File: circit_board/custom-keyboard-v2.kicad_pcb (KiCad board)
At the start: 2 copper layers, 4 parts, among them SW1 SW_Push

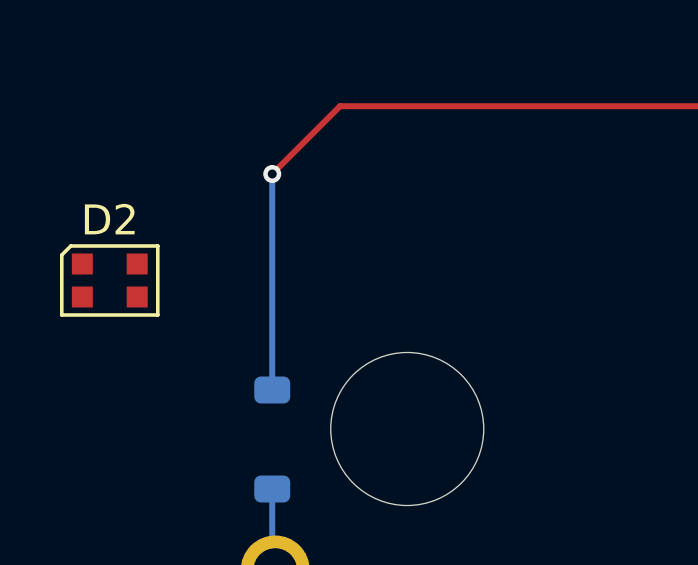
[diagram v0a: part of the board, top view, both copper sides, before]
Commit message: Added instructions for centering an LED + gitignore
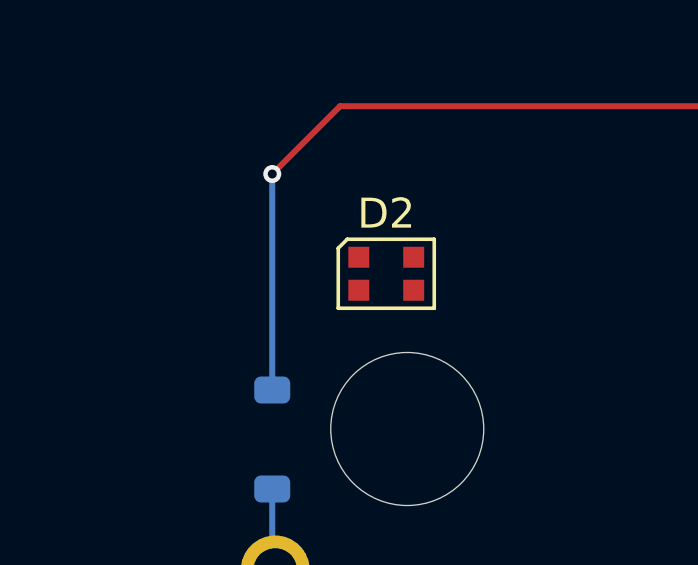
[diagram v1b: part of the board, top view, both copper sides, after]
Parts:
- moved D2 9.22 mm to (122.3, 78.3)
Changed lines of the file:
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@@
 	(footprint "LED_SMD:LED_WS2812B-2020_PLCC4_2.0x2.0mm"
 		(layer "F.Cu")
-		(at 113.085 78.55)
+		(at 122.3 78.325)
 		(descr "2.0mm x 2.0mm Addressable RGB LED NeoPixel Nano, 12 mA, https://cdn-shop.adafruit.com/product-files/4684/4684_WS2812B-2020_V1.3_EN.pdf")
 		(tags "LED RGB NeoPixel Nano PLCC-4 2020")

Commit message: Possitioned keys on circitboard with spacing of 19mm (may change later)
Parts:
- added D10: 1N4148W, Diode_SMD:D_SOD-123, F.Cu at (58.6, 191.1)
- added D11: 1N4148W, Diode_SMD:D_SOD-123, F.Cu at (64.4, 160.9)
- added D12: 1N4148W, Diode_SMD:D_SOD-123, F.Cu at (64.4, 164.3)
- added D13: 1N4148W, Diode_SMD:D_SOD-123, F.Cu at (64.4, 167.7)
- added D14: 1N4148W, Diode_SMD:D_SOD-123, F.Cu at (64.4, 171.0)
- added D15: 1N4148W, Diode_SMD:D_SOD-123, F.Cu at (64.4, 174.3)
- added D16: 1N4148W, Diode_SMD:D_SOD-123, F.Cu at (64.4, 177.7)
- added D17: 1N4148W, Diode_SMD:D_SOD-123, F.Cu at (64.4, 181.1)
- added D18: 1N4148W, Diode_SMD:D_SOD-123, F.Cu at (64.4, 184.4)
- added D19: 1N4148W, Diode_SMD:D_SOD-123, F.Cu at (64.4, 187.8)
- added D20: 1N4148W, Diode_SMD:D_SOD-123, F.Cu at (64.4, 191.1)
- added D21: 1N4148W, Diode_SMD:D_SOD-123, F.Cu at (70.2, 160.9)
- added D22: 1N4148W, Diode_SMD:D_SOD-123, F.Cu at (70.2, 164.3)
- added D23: 1N4148W, Diode_SMD:D_SOD-123, F.Cu at (70.2, 167.7)
- added D24: 1N4148W, Diode_SMD:D_SOD-123, F.Cu at (70.2, 171.0)
- added D25: 1N4148W, Diode_SMD:D_SOD-123, F.Cu at (70.2, 174.3)
- added D26: 1N4148W, Diode_SMD:D_SOD-123, F.Cu at (70.2, 177.7)
- added D27: 1N4148W, Diode_SMD:D_SOD-123, F.Cu at (70.2, 181.1)
- added D28: 1N4148W, Diode_SMD:D_SOD-123, F.Cu at (70.2, 184.4)
- added D29: 1N4148W, Diode_SMD:D_SOD-123, F.Cu at (70.2, 187.8)
- added D3: 1N4148W, Diode_SMD:D_SOD-123, F.Cu at (58.6, 167.7)
- added D30: 1N4148W, Diode_SMD:D_SOD-123, F.Cu at (70.2, 191.1)
- added D31: 1N4148W, Diode_SMD:D_SOD-123, F.Cu at (76.0, 160.9)
- added D32: 1N4148W, Diode_SMD:D_SOD-123, F.Cu at (76.0, 164.3)
- added D33: 1N4148W, Diode_SMD:D_SOD-123, F.Cu at (76.0, 167.7)
- added D34: 1N4148W, Diode_SMD:D_SOD-123, F.Cu at (76.0, 171.0)
- added D35: 1N4148W, Diode_SMD:D_SOD-123, F.Cu at (76.0, 174.3)
- added D36: 1N4148W, Diode_SMD:D_SOD-123, F.Cu at (76.0, 177.7)
- added D37: 1N4148W, Diode_SMD:D_SOD-123, F.Cu at (76.0, 181.1)
- added D38: 1N4148W, Diode_SMD:D_SOD-123, F.Cu at (76.0, 184.4)
- added D39: 1N4148W, Diode_SMD:D_SOD-123, F.Cu at (76.0, 187.8)
- added D4: 1N4148W, Diode_SMD:D_SOD-123, F.Cu at (58.6, 171.0)
- added D40: 1N4148W, Diode_SMD:D_SOD-123, F.Cu at (76.0, 191.1)
- added D41: 1N4148W, Diode_SMD:D_SOD-123, F.Cu at (81.8, 160.9)
- added D42: 1N4148W, Diode_SMD:D_SOD-123, F.Cu at (81.8, 164.3)
- added D43: 1N4148W, Diode_SMD:D_SOD-123, F.Cu at (81.8, 167.7)
- added D44: 1N4148W, Diode_SMD:D_SOD-123, F.Cu at (81.8, 171.0)
- added D45: 1N4148W, Diode_SMD:D_SOD-123, F.Cu at (81.8, 174.3)
- added D46: 1N4148W, Diode_SMD:D_SOD-123, F.Cu at (81.8, 177.7)
- added D5: 1N4148W, Diode_SMD:D_SOD-123, F.Cu at (58.6, 174.3)
- added D6: 1N4148W, Diode_SMD:D_SOD-123, F.Cu at (58.6, 177.7)
- added D7: 1N4148W, Diode_SMD:D_SOD-123, F.Cu at (58.6, 181.1)
- added D8: 1N4148W, Diode_SMD:D_SOD-123, F.Cu at (58.6, 184.4)
- added D9: 1N4148W, Diode_SMD:D_SOD-123, F.Cu at (58.6, 187.8)
- added LED1: WS2812B-2020, LED_SMD:LED_WS2812B-2020_PLCC4_2.0x2.0mm, F.Cu at (86.9, 161.1)
- added LED10: WS2812B-2020, LED_SMD:LED_WS2812B-2020_PLCC4_2.0x2.0mm, F.Cu at (91.2, 164.6)
- added LED11: WS2812B-2020, LED_SMD:LED_WS2812B-2020_PLCC4_2.0x2.0mm, F.Cu at (91.2, 168.2)
- added LED12: WS2812B-2020, LED_SMD:LED_WS2812B-2020_PLCC4_2.0x2.0mm, F.Cu at (91.2, 171.7)
- added LED13: WS2812B-2020, LED_SMD:LED_WS2812B-2020_PLCC4_2.0x2.0mm, F.Cu at (91.2, 175.2)
- added LED14: WS2812B-2020, LED_SMD:LED_WS2812B-2020_PLCC4_2.0x2.0mm, F.Cu at (91.2, 178.8)
- added LED15: WS2812B-2020, LED_SMD:LED_WS2812B-2020_PLCC4_2.0x2.0mm, F.Cu at (91.2, 182.3)
- added LED16: WS2812B-2020, LED_SMD:LED_WS2812B-2020_PLCC4_2.0x2.0mm, F.Cu at (91.2, 185.9)
- added LED17: WS2812B-2020, LED_SMD:LED_WS2812B-2020_PLCC4_2.0x2.0mm, F.Cu at (95.5, 161.1)
- added LED18: WS2812B-2020, LED_SMD:LED_WS2812B-2020_PLCC4_2.0x2.0mm, F.Cu at (95.5, 164.6)
- added LED19: WS2812B-2020, LED_SMD:LED_WS2812B-2020_PLCC4_2.0x2.0mm, F.Cu at (95.5, 168.2)
- added LED2: WS2812B-2020, LED_SMD:LED_WS2812B-2020_PLCC4_2.0x2.0mm, F.Cu at (86.9, 164.6)
- added LED20: WS2812B-2020, LED_SMD:LED_WS2812B-2020_PLCC4_2.0x2.0mm, F.Cu at (95.5, 171.7)
- added LED21: WS2812B-2020, LED_SMD:LED_WS2812B-2020_PLCC4_2.0x2.0mm, F.Cu at (95.5, 175.2)
- added LED22: WS2812B-2020, LED_SMD:LED_WS2812B-2020_PLCC4_2.0x2.0mm, F.Cu at (95.5, 178.8)
- added LED23: WS2812B-2020, LED_SMD:LED_WS2812B-2020_PLCC4_2.0x2.0mm, F.Cu at (95.5, 182.3)
- added LED24: WS2812B-2020, LED_SMD:LED_WS2812B-2020_PLCC4_2.0x2.0mm, F.Cu at (95.5, 185.9)
- added LED25: WS2812B-2020, LED_SMD:LED_WS2812B-2020_PLCC4_2.0x2.0mm, F.Cu at (99.8, 161.1)
- added LED26: WS2812B-2020, LED_SMD:LED_WS2812B-2020_PLCC4_2.0x2.0mm, F.Cu at (99.8, 164.6)
- added LED27: WS2812B-2020, LED_SMD:LED_WS2812B-2020_PLCC4_2.0x2.0mm, F.Cu at (99.8, 168.2)
- added LED28: WS2812B-2020, LED_SMD:LED_WS2812B-2020_PLCC4_2.0x2.0mm, F.Cu at (99.8, 171.7)
- added LED29: WS2812B-2020, LED_SMD:LED_WS2812B-2020_PLCC4_2.0x2.0mm, F.Cu at (99.8, 175.2)
- added LED3: WS2812B-2020, LED_SMD:LED_WS2812B-2020_PLCC4_2.0x2.0mm, F.Cu at (86.9, 168.2)
- added LED30: WS2812B-2020, LED_SMD:LED_WS2812B-2020_PLCC4_2.0x2.0mm, F.Cu at (99.8, 178.8)
- added LED31: WS2812B-2020, LED_SMD:LED_WS2812B-2020_PLCC4_2.0x2.0mm, F.Cu at (99.8, 182.3)
- added LED32: WS2812B-2020, LED_SMD:LED_WS2812B-2020_PLCC4_2.0x2.0mm, F.Cu at (99.8, 185.9)
- added LED33: WS2812B-2020, LED_SMD:LED_WS2812B-2020_PLCC4_2.0x2.0mm, F.Cu at (104.1, 161.1)
- added LED34: WS2812B-2020, LED_SMD:LED_WS2812B-2020_PLCC4_2.0x2.0mm, F.Cu at (104.1, 164.6)
- added LED35: WS2812B-2020, LED_SMD:LED_WS2812B-2020_PLCC4_2.0x2.0mm, F.Cu at (104.1, 168.2)
- added LED36: WS2812B-2020, LED_SMD:LED_WS2812B-2020_PLCC4_2.0x2.0mm, F.Cu at (104.1, 171.7)
- added LED37: WS2812B-2020, LED_SMD:LED_WS2812B-2020_PLCC4_2.0x2.0mm, F.Cu at (104.1, 175.2)
- added LED38: WS2812B-2020, LED_SMD:LED_WS2812B-2020_PLCC4_2.0x2.0mm, F.Cu at (104.1, 178.8)
- added LED39: WS2812B-2020, LED_SMD:LED_WS2812B-2020_PLCC4_2.0x2.0mm, F.Cu at (104.1, 182.3)
- added LED4: WS2812B-2020, LED_SMD:LED_WS2812B-2020_PLCC4_2.0x2.0mm, F.Cu at (86.9, 171.7)
- added LED40: WS2812B-2020, LED_SMD:LED_WS2812B-2020_PLCC4_2.0x2.0mm, F.Cu at (104.1, 185.9)
- added LED41: WS2812B-2020, LED_SMD:LED_WS2812B-2020_PLCC4_2.0x2.0mm, F.Cu at (108.5, 161.1)
- added LED42: WS2812B-2020, LED_SMD:LED_WS2812B-2020_PLCC4_2.0x2.0mm, F.Cu at (108.5, 164.6)
- added LED43: WS2812B-2020, LED_SMD:LED_WS2812B-2020_PLCC4_2.0x2.0mm, F.Cu at (108.5, 168.2)
- added LED44: WS2812B-2020, LED_SMD:LED_WS2812B-2020_PLCC4_2.0x2.0mm, F.Cu at (108.5, 171.7)
- added LED45: WS2812B-2020, LED_SMD:LED_WS2812B-2020_PLCC4_2.0x2.0mm, F.Cu at (108.5, 175.2)
- added LED46: WS2812B-2020, LED_SMD:LED_WS2812B-2020_PLCC4_2.0x2.0mm, F.Cu at (108.5, 178.8)
- added LED5: WS2812B-2020, LED_SMD:LED_WS2812B-2020_PLCC4_2.0x2.0mm, F.Cu at (86.9, 175.2)
- added LED6: WS2812B-2020, LED_SMD:LED_WS2812B-2020_PLCC4_2.0x2.0mm, F.Cu at (86.9, 178.8)
- added LED7: WS2812B-2020, LED_SMD:LED_WS2812B-2020_PLCC4_2.0x2.0mm, F.Cu at (86.9, 182.3)
- added LED8: WS2812B-2020, LED_SMD:LED_WS2812B-2020_PLCC4_2.0x2.0mm, F.Cu at (86.9, 185.9)
- added LED9: WS2812B-2020, LED_SMD:LED_WS2812B-2020_PLCC4_2.0x2.0mm, F.Cu at (91.2, 161.1)
- added SW10: SW_Push, MX_V2:Gateron-KS33-Solderable-Template, F.Cu at (266.0, 57.0)
- added SW11: SW_Push, MX_V2:Gateron-KS33-Solderable-Template, F.Cu at (38.0, 76.0)
- added SW12: SW_Push, MX_V2:Gateron-KS33-Solderable-Template, F.Cu at (57.0, 76.0)
- added SW13: SW_Push, MX_V2:Gateron-KS33-Solderable-Template, F.Cu at (76.0, 76.0)
- added SW14: SW_Push, MX_V2:Gateron-KS33-Solderable-Template, F.Cu at (95.0, 76.0)
- added SW15: SW_Push, MX_V2:Gateron-KS33-Solderable-Template, F.Cu at (114.0, 76.0)
- added SW16: SW_Push, MX_V2:Gateron-KS33-Solderable-Template, F.Cu at (190.0, 76.0)
- added SW17: SW_Push, MX_V2:Gateron-KS33-Solderable-Template, F.Cu at (209.0, 76.0)
- added SW18: SW_Push, MX_V2:Gateron-KS33-Solderable-Template, F.Cu at (228.0, 76.0)
- added SW19: SW_Push, MX_V2:Gateron-KS33-Solderable-Template, F.Cu at (247.0, 76.0)
- added SW2: SW_Push, MX_V2:Gateron-KS33-Solderable-Template, F.Cu at (57.0, 57.0)
- added SW20: SW_Push, MX_V2:Gateron-KS33-Solderable-Template, F.Cu at (266.0, 76.0)
- added SW21: SW_Push, MX_V2:Gateron-KS33-Solderable-Template, F.Cu at (38.0, 95.0)
- added SW22: SW_Push, MX_V2:Gateron-KS33-Solderable-Template, F.Cu at (57.0, 95.0)
- added SW23: SW_Push, MX_V2:Gateron-KS33-Solderable-Template, F.Cu at (76.0, 95.0)
- added SW24: SW_Push, MX_V2:Gateron-KS33-Solderable-Template, F.Cu at (95.0, 95.0)
- added SW25: SW_Push, MX_V2:Gateron-KS33-Solderable-Template, F.Cu at (114.0, 95.0)
- added SW26: SW_Push, MX_V2:Gateron-KS33-Solderable-Template, F.Cu at (190.0, 95.0)
- added SW27: SW_Push, MX_V2:Gateron-KS33-Solderable-Template, F.Cu at (209.0, 95.0)
- added SW28: SW_Push, MX_V2:Gateron-KS33-Solderable-Template, F.Cu at (228.0, 95.0)
- added SW29: SW_Push, MX_V2:Gateron-KS33-Solderable-Template, F.Cu at (247.0, 95.0)
- added SW3: SW_Push, MX_V2:Gateron-KS33-Solderable-Template, F.Cu at (76.0, 57.0)
- added SW30: SW_Push, MX_V2:Gateron-KS33-Solderable-Template, F.Cu at (266.0, 95.0)
- added SW31: SW_Push, MX_V2:Gateron-KS33-Solderable-Template, F.Cu at (38.0, 114.0)
- added SW32: SW_Push, MX_V2:Gateron-KS33-Solderable-Template, F.Cu at (57.0, 114.0)
- added SW33: SW_Push, MX_V2:Gateron-KS33-Solderable-Template, F.Cu at (76.0, 114.0)
- added SW34: SW_Push, MX_V2:Gateron-KS33-Solderable-Template, F.Cu at (95.0, 114.0)
- added SW35: SW_Push, MX_V2:Gateron-KS33-Solderable-Template, F.Cu at (114.0, 114.0)
- added SW36: SW_Push, MX_V2:Gateron-KS33-Solderable-Template, F.Cu at (190.0, 114.0)
- added SW37: SW_Push, MX_V2:Gateron-KS33-Solderable-Template, F.Cu at (209.0, 114.0)
- added SW38: SW_Push, MX_V2:Gateron-KS33-Solderable-Template, F.Cu at (228.0, 114.0)
- added SW39: SW_Push, MX_V2:Gateron-KS33-Solderable-Template, F.Cu at (247.0, 114.0)
- added SW4: SW_Push, MX_V2:Gateron-KS33-Solderable-Template, F.Cu at (95.0, 57.0)
- added SW40: SW_Push, MX_V2:Gateron-KS33-Solderable-Template, F.Cu at (266.0, 114.0)
- added SW41: SW_Push, MX_V2:Gateron-KS33-Solderable-Template, F.Cu at (76.0, 133.0)
- added SW42: SW_Push, MX_V2:Gateron-KS33-Solderable-Template, F.Cu at (95.0, 133.0)
- added SW43: SW_Push, MX_V2:Gateron-KS33-Solderable-Template, F.Cu at (114.0, 133.0)
- added SW44: SW_Push, MX_V2:Gateron-KS33-Solderable-Template, F.Cu at (190.0, 133.0)
- added SW45: SW_Push, MX_V2:Gateron-KS33-Solderable-Template, F.Cu at (209.0, 133.0)
- added SW46: SW_Push, MX_V2:Gateron-KS33-Solderable-Template, F.Cu at (228.0, 133.0)
- added SW5: SW_Push, MX_V2:Gateron-KS33-Solderable-Template, F.Cu at (114.0, 57.0)
- added SW6: SW_Push, MX_V2:Gateron-KS33-Solderable-Template, F.Cu at (190.0, 57.0)
- added SW7: SW_Push, MX_V2:Gateron-KS33-Solderable-Template, F.Cu at (209.0, 57.0)
- added SW8: SW_Push, MX_V2:Gateron-KS33-Solderable-Template, F.Cu at (228.0, 57.0)
- added SW9: SW_Push, MX_V2:Gateron-KS33-Solderable-Template, F.Cu at (247.0, 57.0)
- D1: moved to F.Cu
- D2: value WS2812B-2020 -> 1N4148W; footprint LED_SMD:LED_WS2812B-2020_PLCC4_2.0x2.0mm -> Diode_SMD:D_SOD-123
- moved D2 107.0 mm to (58.6, 164.3)
- moved D1 97.6 mm to (58.6, 160.9), turned to 0 degrees
- moved SW1 89.0 mm to (38.0, 57.0)
- moved A1 21.6 mm to (152.0, 76.0)
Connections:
- A1 pad 1: Net-(A1-GPIO0) -> col1
- A1 pad 10: unconnected-(A1-GPIO7-Pad10) -> col8
- A1 pad 11: unconnected-(A1-GPIO8-Pad11) -> col9
- A1 pad 12: unconnected-(A1-GPIO9-Pad12) -> col10
- A1 pad 13: Net-(A1-GND-Pad13) -> gnd
- A1 pad 14: unconnected-(A1-GPIO10-Pad14) -> row1
- A1 pad 15: unconnected-(A1-GPIO11-Pad15) -> row2
- A1 pad 16: unconnected-(A1-GPIO12-Pad16) -> row3
- A1 pad 17: unconnected-(A1-GPIO13-Pad17) -> row4
- A1 pad 18: Net-(A1-GND-Pad13) -> gnd
- A1 pad 19: unconnected-(A1-GPIO14-Pad19) -> row5
- A1 pad 2: unconnected-(A1-GPIO1-Pad2) -> col2
- A1 pad 20: unconnected-(A1-GPIO15-Pad20) -> led-data
- A1 pad 23: Net-(A1-GND-Pad13) -> gnd
- A1 pad 28: Net-(A1-GND-Pad13) -> gnd
- A1 pad 3: Net-(A1-GND-Pad13) -> gnd
- A1 pad 38: Net-(A1-GND-Pad13) -> gnd
- A1 pad 4: unconnected-(A1-GPIO2-Pad4) -> col3
- A1 pad 40: unconnected-(A1-VBUS-Pad40) -> led-power
- A1 pad 5: unconnected-(A1-GPIO3-Pad5) -> col4
- A1 pad 6: unconnected-(A1-GPIO4-Pad6) -> col5
- A1 pad 7: unconnected-(A1-GPIO5-Pad7) -> col6
- A1 pad 8: Net-(A1-GND-Pad13) -> gnd
- A1 pad 9: unconnected-(A1-GPIO6-Pad9) -> col7
- D1 pad 1: Net-(D1-K) -> row1
- D1 pad 2: Net-(A1-GPIO0) -> Net-(D1-A)
- D2 pad 1: unconnected-(D2-DOUT-Pad1) -> row1
- D2 pad 2: unconnected-(D2-VSS-Pad2) -> Net-(D2-A)
- SW1 pad 1: Net-(D1-K) -> col1
- SW1 pad 2: Net-(A1-GND-Pad13) -> Net-(D1-A)
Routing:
- net Net-(A1-GPIO0): track 26.6 -> 0.00 mm, vias 1 -> 0
- net Net-(A1-GND-Pad13): track 11.8 -> 0.00 mm
- net Net-(D1-K): track 2.74 -> 0.00 mm

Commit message: Positioned dioes on circit board
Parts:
- D1, D10, D11, D12, D13, D14, D15, D16, D17, D18, D19, D2, D20, D21, D22, D23, D24, D25, D26, D27, D28, D29, D3, D30, D31, D32, D33, D34, D35, D36, D37, D38, D39, D4, D40, D41, D42, D43, D44, D45, D46, D5, D6, D7, D8, D9: moved to B.Cu
- moved D10 304.7 mm to (346.8, 91.9), turned to -90 degrees
- moved D20 293.5 mm to (346.8, 110.9), turned to -90 degrees
- moved D9 285.7 mm to (327.8, 91.9), turned to -90 degrees
- moved D30 283.2 mm to (346.8, 129.9), turned to -90 degrees
- moved D19 274.3 mm to (327.8, 110.9), turned to -90 degrees
- moved D40 274.0 mm to (346.8, 148.9), turned to -90 degrees
- moved D8 266.7 mm to (308.8, 91.9), turned to -90 degrees
- moved D29 263.9 mm to (327.8, 129.9), turned to -90 degrees
- moved D18 255.1 mm to (308.8, 110.9), turned to -90 degrees
- moved D39 254.7 mm to (327.8, 148.9), turned to -90 degrees
- moved D7 247.7 mm to (289.8, 91.9), turned to -90 degrees
- moved D28 244.7 mm to (308.8, 129.9), turned to -90 degrees
- moved D17 236.0 mm to (289.8, 110.9), turned to -90 degrees
- moved D38 235.4 mm to (308.8, 148.9), turned to -90 degrees
- moved D6 228.8 mm to (270.8, 91.9), turned to -90 degrees
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
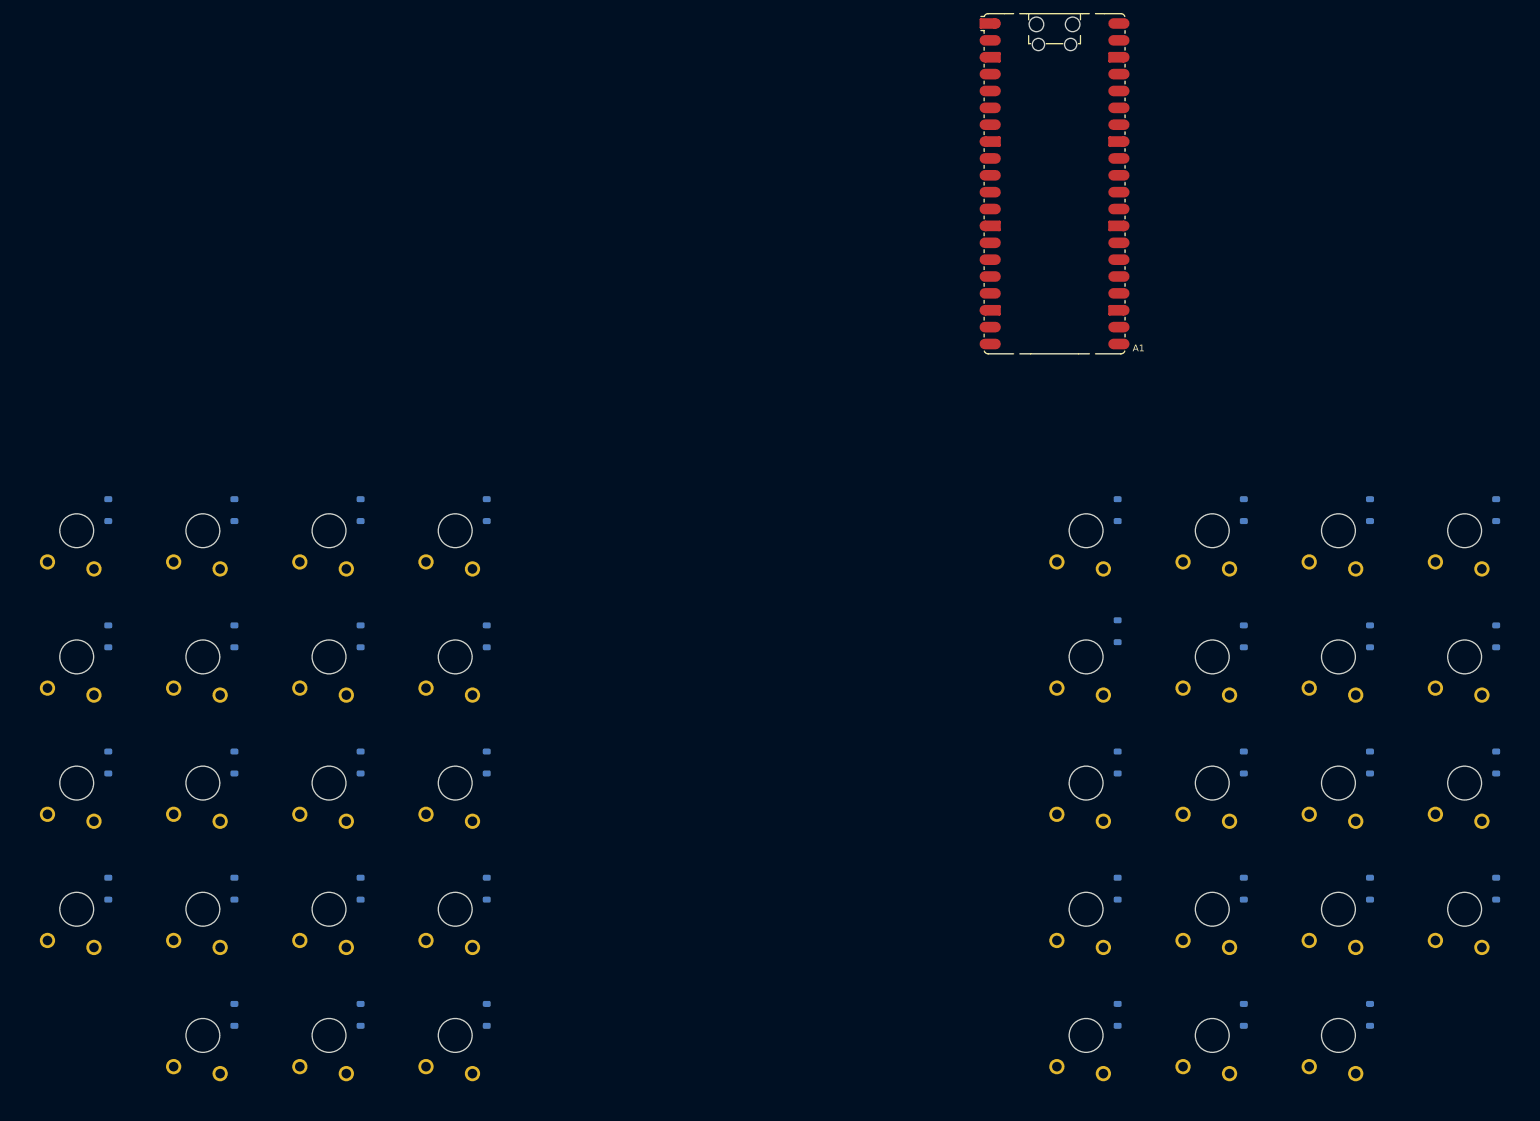
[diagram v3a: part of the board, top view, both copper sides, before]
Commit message: Added vertical offset to keys
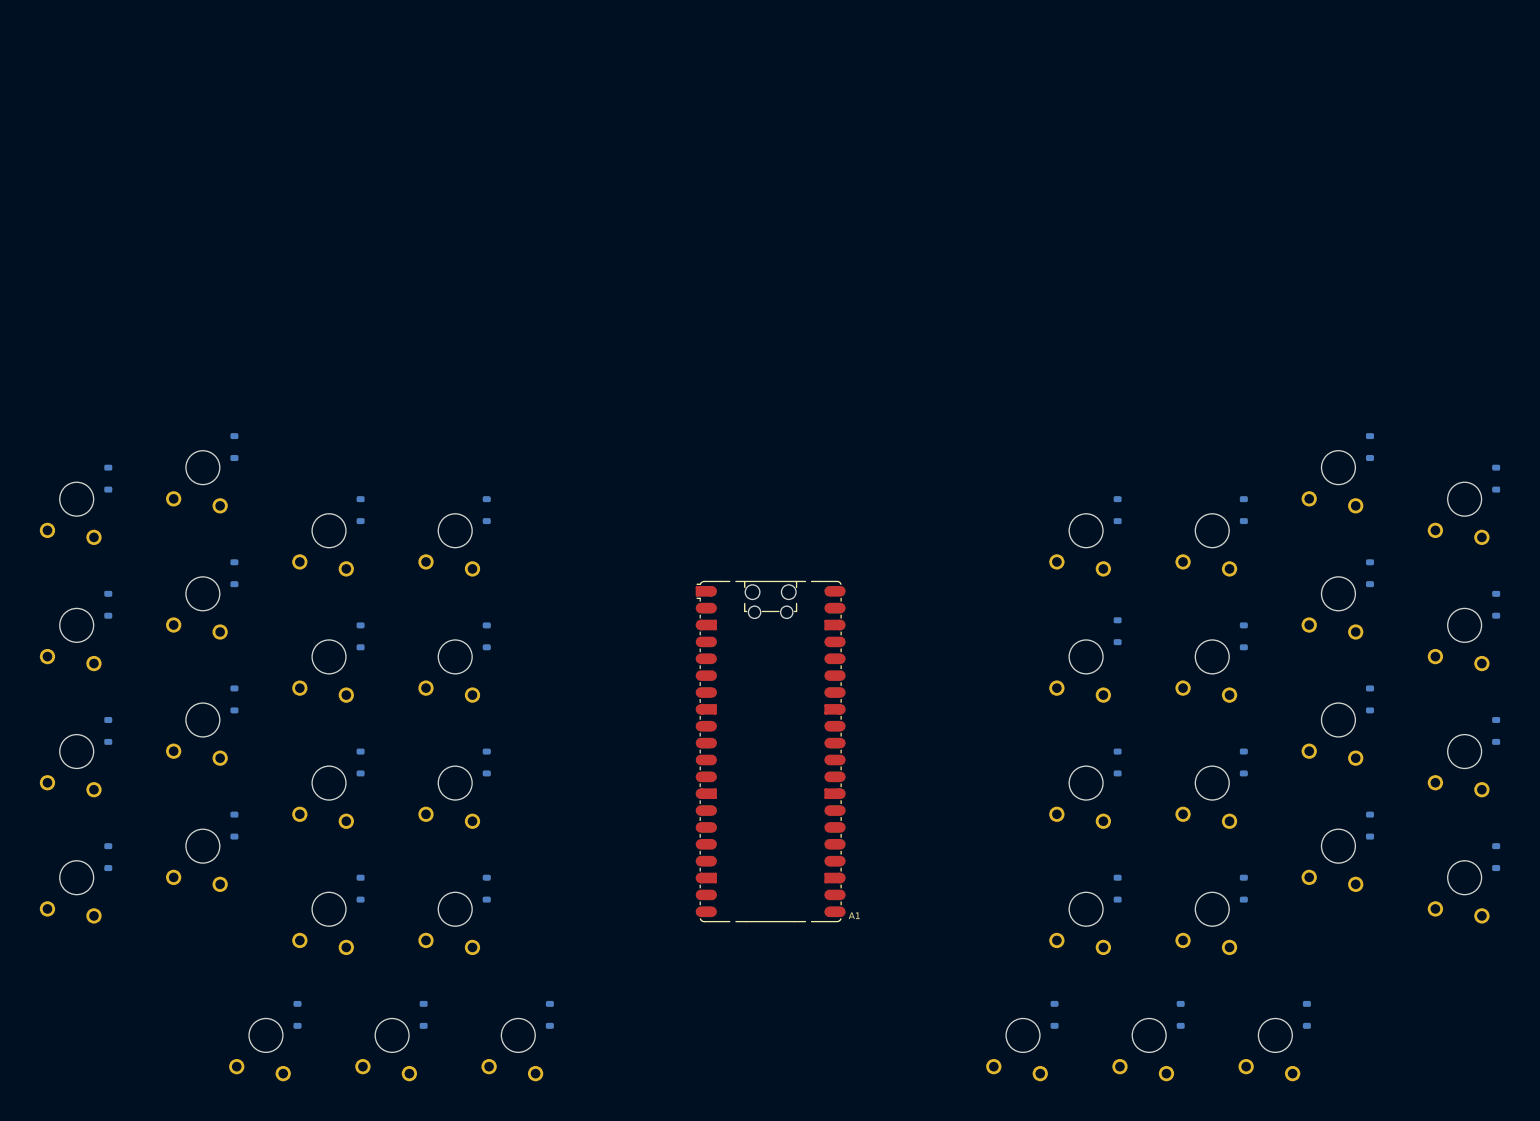
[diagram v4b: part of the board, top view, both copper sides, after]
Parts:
- moved A1 95.6 mm to (218.5, 128.2)
- moved D13 9.50 mm to (137.8, 101.4)
- moved D18 9.50 mm to (308.8, 101.4)
- moved D23 9.50 mm to (137.8, 120.4)
- moved D28 9.50 mm to (308.8, 120.4)
- moved D3 9.50 mm to (137.8, 82.4)
- moved D33 9.50 mm to (137.8, 139.4)
- moved D38 9.50 mm to (308.8, 139.4)
- moved D41 9.50 mm to (147.2, 167.9)
- moved D42 9.50 mm to (166.2, 167.9)
- moved D43 9.50 mm to (185.2, 167.9)
- moved D44 9.50 mm to (261.2, 167.9)
- moved D45 9.50 mm to (280.2, 167.9)
- moved D46 9.50 mm to (299.2, 167.9)
- moved D8 9.50 mm to (308.8, 82.4)
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
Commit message: Added edge cuts + repositioned pi pico
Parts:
- moved A1 21.6 mm to (218.5, 106.7)
- moved D1 4.75 mm to (99.8, 96.7)
- moved D10 4.75 mm to (346.8, 96.7)
- moved D11 4.75 mm to (99.8, 115.7)
- moved D12 4.75 mm to (118.8, 110.9)
- moved D13 4.75 mm to (137.8, 106.2)
- moved D18 4.75 mm to (308.8, 106.2)
- moved D19 4.75 mm to (327.8, 110.9)
- moved D2 4.75 mm to (118.8, 91.9)
- moved D20 4.75 mm to (346.8, 115.7)
- moved D21 4.75 mm to (99.8, 134.7)
- moved D22 4.75 mm to (118.8, 129.9)
- moved D23 4.75 mm to (137.8, 125.2)
- moved D28 4.75 mm to (308.8, 125.2)
- moved D29 4.75 mm to (327.8, 129.9)
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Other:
- board outline added: 266 x 99.8 mm

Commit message: Positioned the LEDs on the PCB
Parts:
- moved LED10 205.5 mm to (342.0, 94.6)
- moved LED8 198.0 mm to (304.0, 85.1)
- moved LED20 195.7 mm to (342.0, 113.6)
- moved LED9 190.3 mm to (323.0, 89.8)
- moved LED30 186.3 mm to (342.0, 132.6)
- moved LED19 180.1 mm to (323.0, 108.8)
- moved LED7 178.8 mm to (285.0, 89.8)
- moved LED40 177.3 mm to (342.0, 151.6)
- moved LED29 170.2 mm to (323.0, 127.8)
- moved LED18 165.1 mm to (304.0, 104.1)
- moved LED6 163.6 mm to (266.0, 89.8)
- moved LED39 160.7 mm to (323.0, 146.8)
- moved LED28 154.7 mm to (304.0, 123.1)
- moved LED16 151.7 mm to (266.0, 108.8)
- moved LED17 145.0 mm to (285.0, 108.8)
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
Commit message: Added I2C OLED display
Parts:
- added J1: i2c_display, Connector_PinHeader_2.54mm:PinHeader_1x04_P2.54mm_Vertical, F.Cu at (214.7, 142.5)
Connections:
- A1 pad 21: unconnected-(A1-GPIO16-Pad21) -> I2C-SDA
- A1 pad 22: unconnected-(A1-GPIO17-Pad22) -> I2C-SCL
- A1 pad 36: unconnected-(A1-3V3-Pad36) -> OLED-power
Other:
- board text added: "3v3"
- board text added: "GND"
- board text added: "SCL"
- board text added: "SDA"

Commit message: Began wiring the keyboard matrix, got distracted by 3v -> 5v converters
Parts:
- moved D16 0.77 mm to (270.8, 110.9)
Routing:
- net row4: track 0.00 -> 289.6 mm, vias 0 -> 1
- net row1: track 0.00 -> 287.0 mm, vias 0 -> 1
- net row2: track 0.00 -> 272.2 mm, vias 0 -> 1
- net row3: track 0.00 -> 268.2 mm, vias 0 -> 1
- net row5: track 0.00 -> 193.8 mm, vias 0 -> 1
- net Net-(D5-A): track 0.00 -> 8.09 mm
- net Net-(D4-A): track 0.00 -> 8.09 mm
- net Net-(D3-A): track 0.00 -> 8.09 mm
- net Net-(D23-A): track 0.00 -> 8.09 mm
- net Net-(D2-A): track 0.00 -> 8.09 mm
- net Net-(D15-A): track 0.00 -> 8.09 mm
- net Net-(D14-A): track 0.00 -> 8.09 mm
- net Net-(D13-A): track 0.00 -> 8.09 mm
- net Net-(D12-A): track 0.00 -> 8.09 mm
- net Net-(D11-A): track 0.00 -> 8.09 mm
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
